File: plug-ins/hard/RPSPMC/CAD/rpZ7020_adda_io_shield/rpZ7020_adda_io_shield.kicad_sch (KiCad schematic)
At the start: 31 parts, among them J1 Samtec_ASP-134486-01, J2 Conn_01x03_Socket, J2-FMC-RP1 Conn_02x20, J2-PWR3 Conn_01x03_Pin, J3-FMC-POWER1 Conn_02x06_Odd_Even, J3-PWR12 Conn_01x02_Pin, J4-FMC-AUX1 Conn_02x06_Odd_Even, U1 TC7QPB9306FK, U2 TC7QPB9306FK, U3 TC7QPB9306FK

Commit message: work on SPI
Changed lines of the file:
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@@
 	(wire
 		(pts
+			(xy 226.06 128.27) (xy 232.41 128.27)
+		)
+		(stroke
+			(width 0)
+			(type default)
+		)
+	)
+	(wire
+		(pts
 			(xy 266.7 6.35) (xy 260.35 6.35)
 		)
@@
 	(global_label "RESET FMC"
 		(shape input)
-		(at 232.41 128.27 180)
+		(at 226.06 128.27 180)
 		(fields_autoplaced yes)
 		(effects
@@
 		)
 		(property "Intersheetrefs" "${INTERSHEET_REFS}"
-			(at 218.9021 128.27 0)
+			(at 212.5521 128.27 0)
 			(effects
 				(font

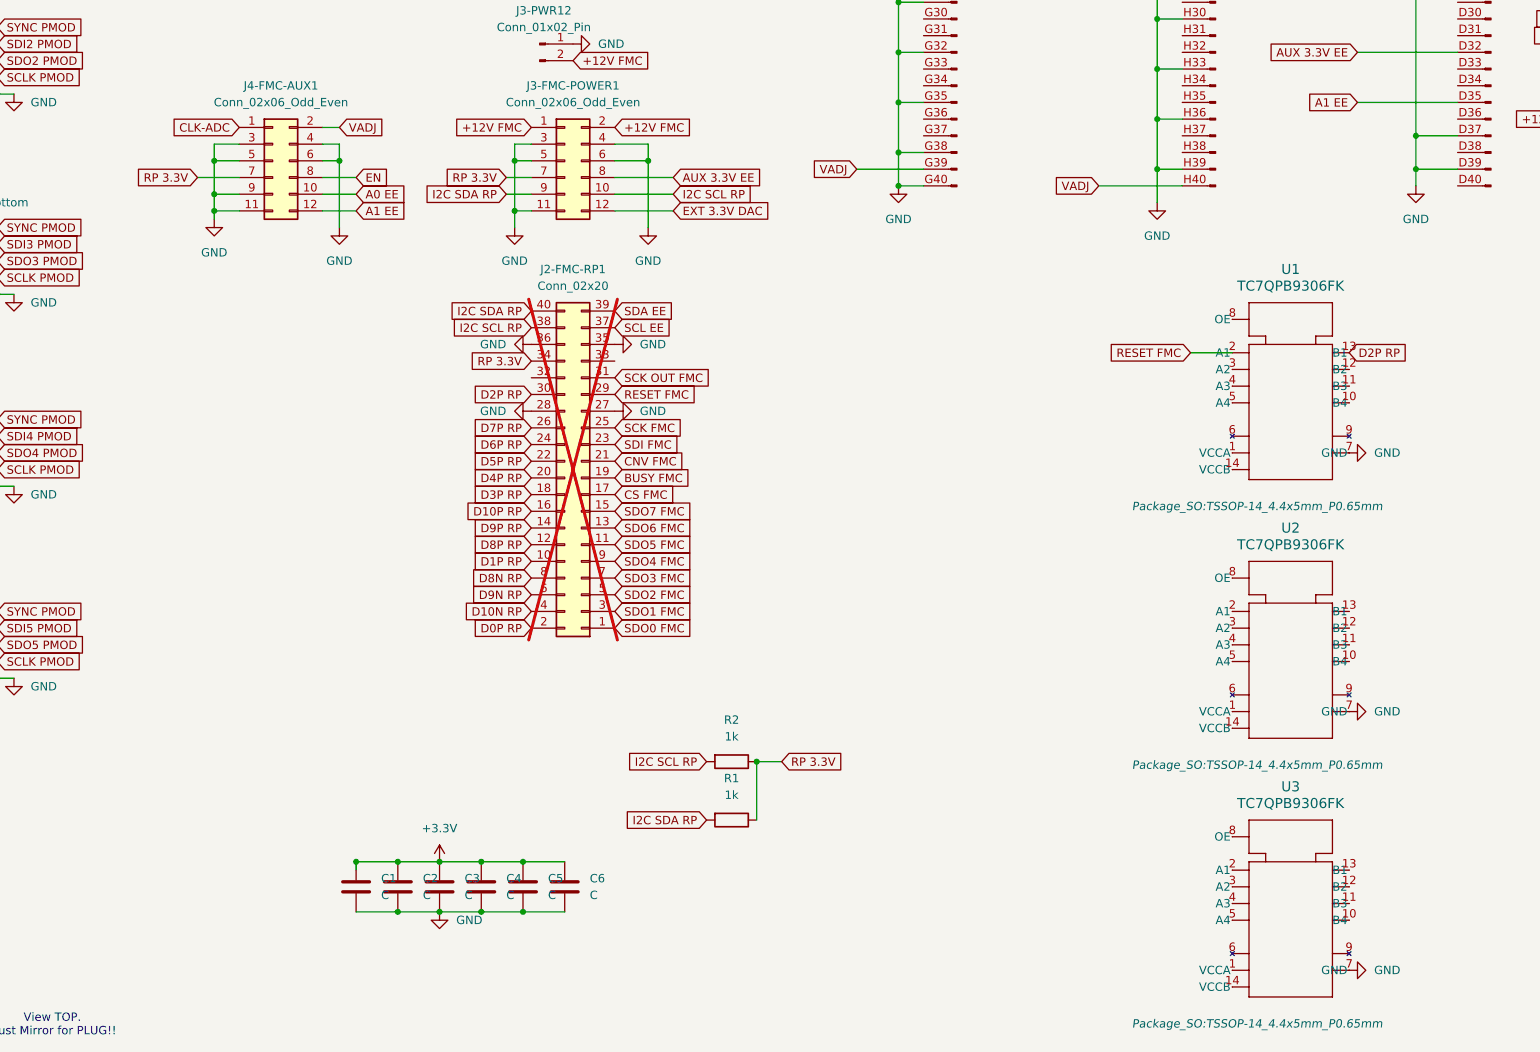
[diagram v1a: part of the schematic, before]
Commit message: updated PCB: Vadj --- 3.3V
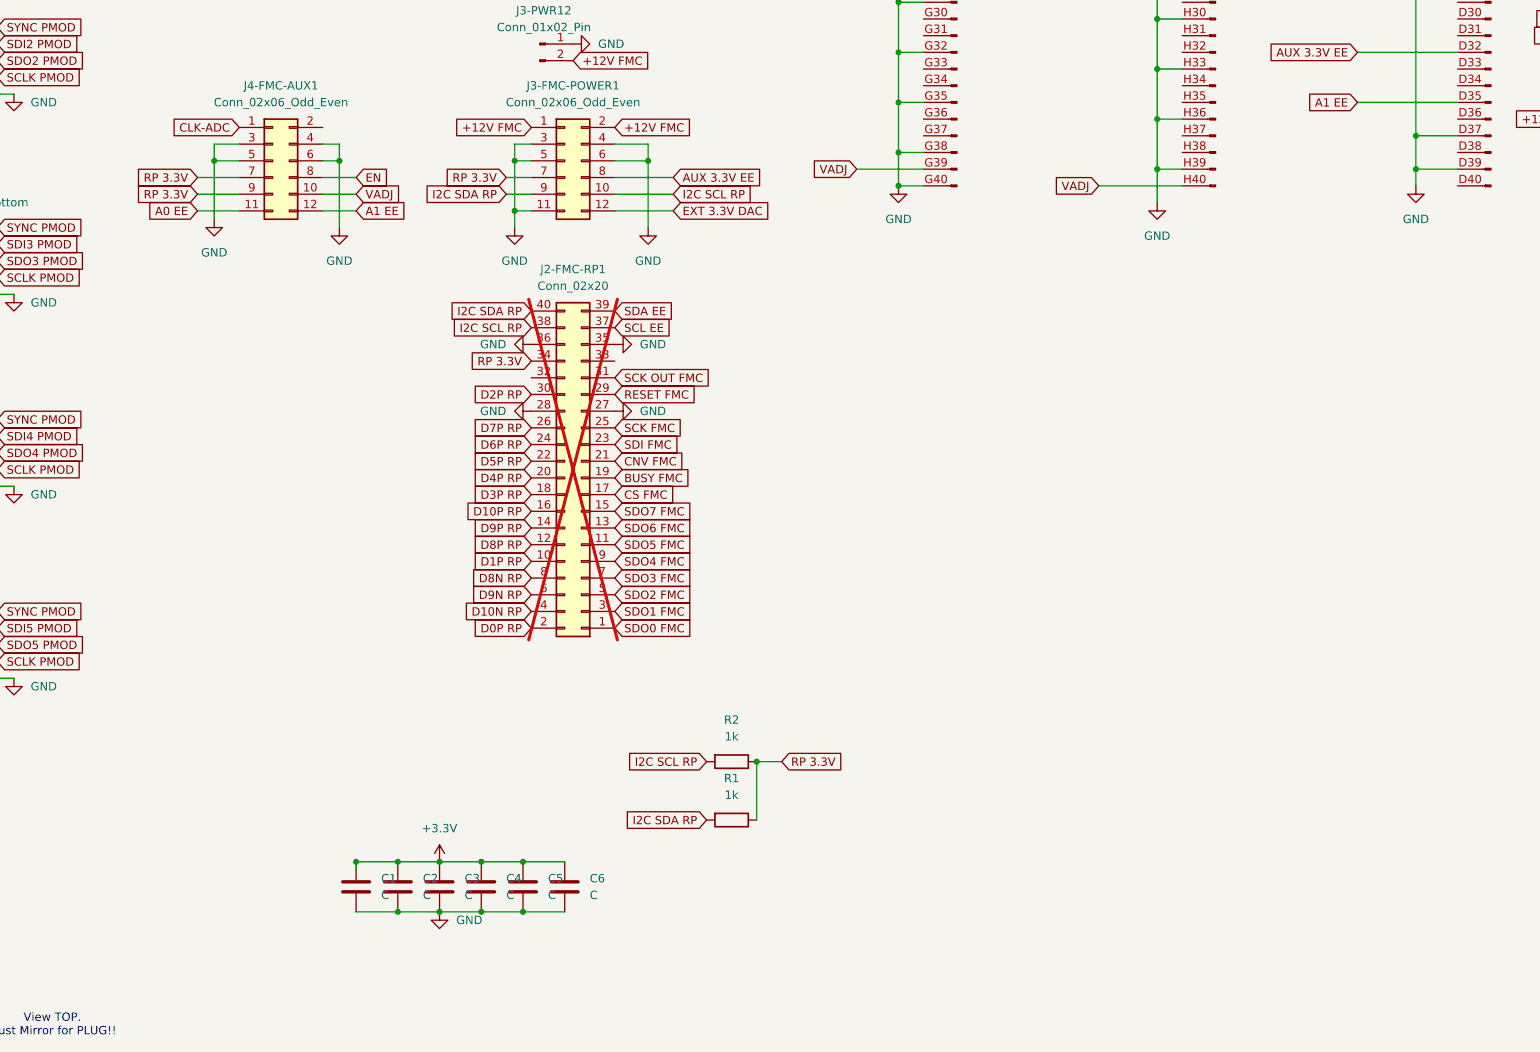
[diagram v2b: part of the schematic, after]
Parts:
- removed U1, U2, U3: TC7QPB9306FK, Package_SO:TSSOP-14_4.4x5mm_P0.65mm, symbol 2025-03-03_01-11-22:TC7QPB9306FK
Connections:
- net A0 EE: now also J4-FMC-AUX1.11 (Pin_11); no longer J4-FMC-AUX1.10 (Pin_10)
- net GND: no longer J4-FMC-AUX1.11 (Pin_11), J4-FMC-AUX1.9 (Pin_9)
- net RP 3.3V: now also J4-FMC-AUX1.9 (Pin_9)
- net VADJ: now also J4-FMC-AUX1.10 (Pin_10); no longer J4-FMC-AUX1.2 (Pin_2)

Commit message: last tweaks before order rev 1.0.1 PCB
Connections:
- net VADJ: now also J2-FMC-RP1.33 (Pin_33)
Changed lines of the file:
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@@
+	(global_label "VADJ"
+		(shape input)
+		(at 138.43 129.54 0)
+		(fields_autoplaced yes)
+		(effects
+			(font
+				(size 1.27 1.27)
+			)
+			(justify left)
+		)
+		(property "Intersheetrefs" "${INTERSHEET_REFS}"
+			(at 145.83 129.54 0)
+			(effects
+				(font
+					(size 1.27 1.27)
+				)
+				(justify left)
+				(hide yes)
+			)
+		)
+	)
 	(global_label "VADJ"
 		(shape input)
